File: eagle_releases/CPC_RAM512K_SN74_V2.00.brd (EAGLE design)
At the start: 99.1 x 81.3 mm, 19 parts

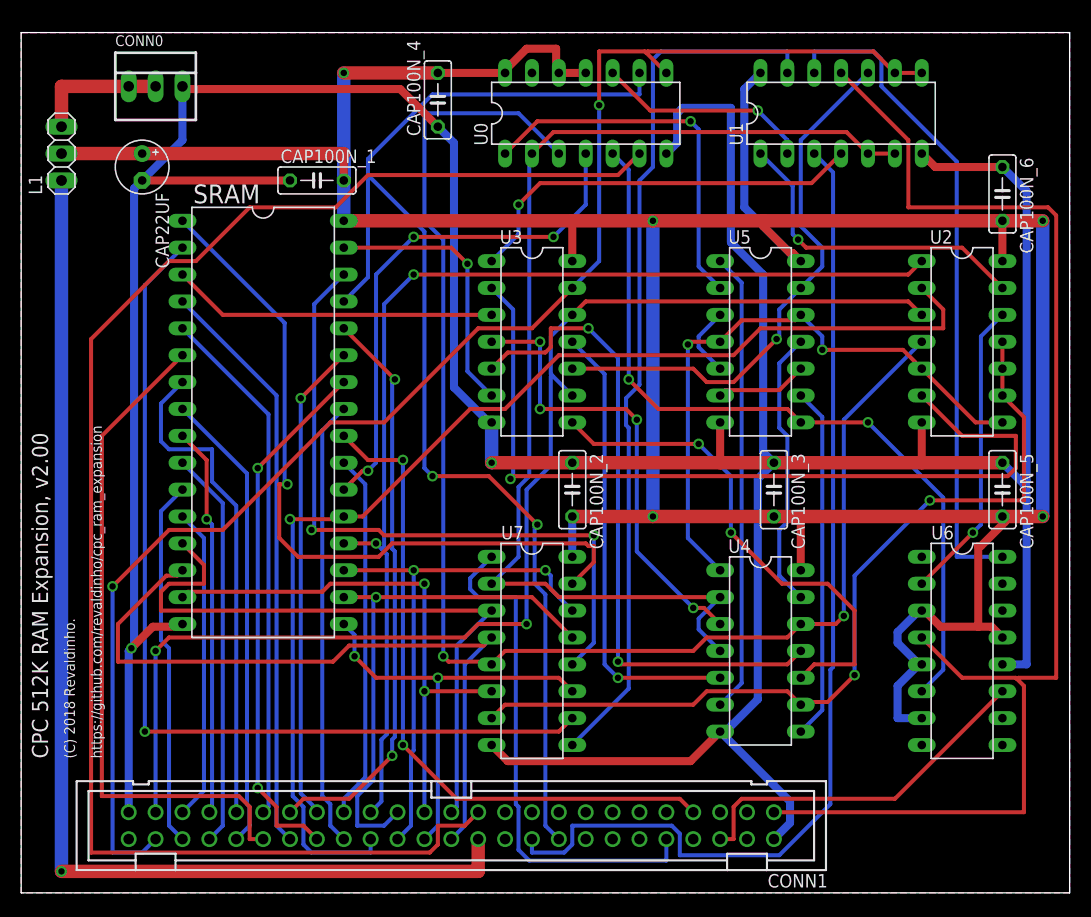
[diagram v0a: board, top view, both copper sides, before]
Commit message: Manual tweaks to 74XX board, mainly power improvements
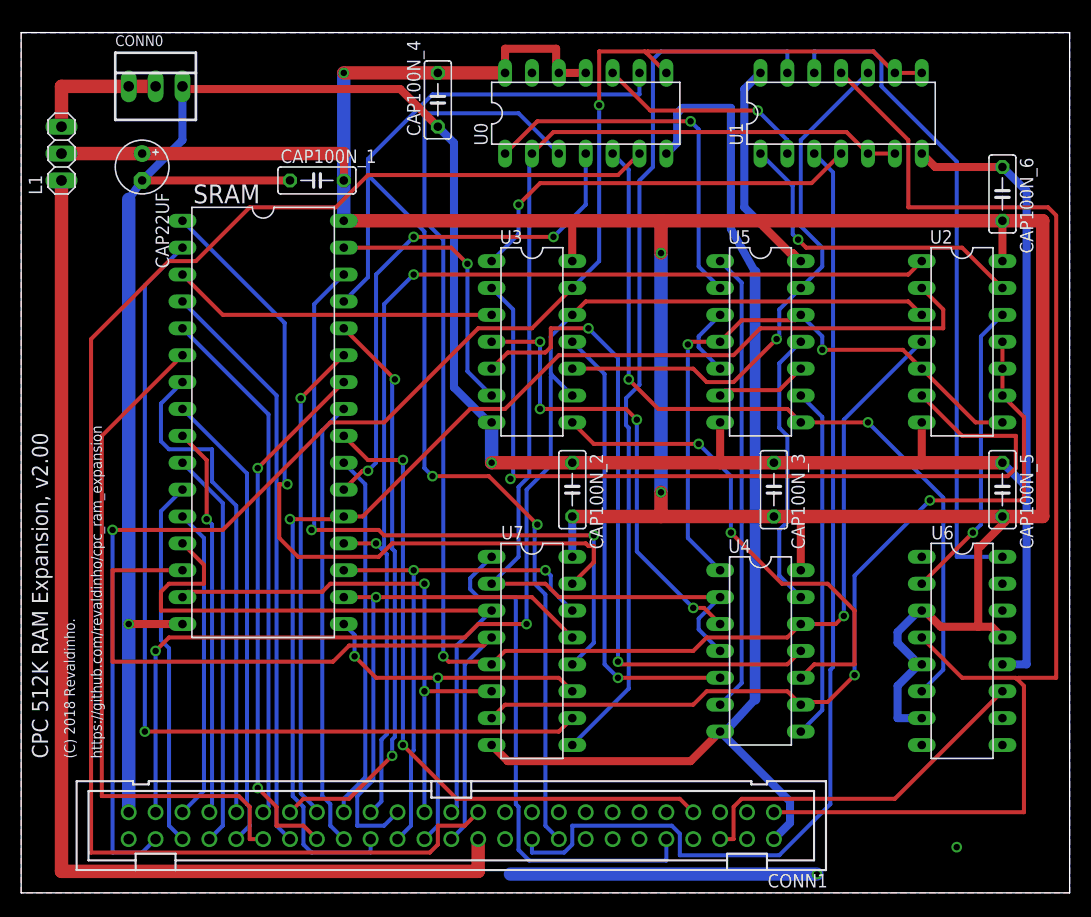
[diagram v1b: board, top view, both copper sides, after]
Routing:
- net VSS: track 376.9 -> 404.9 mm, vias 2 -> 4
- net D1: track 68.6 -> 72.6 mm
- net A15: track 142.4 -> 145.5 mm
- net VDD: track 316.9 -> 318.1 mm, vias 5 -> 3
- net VDD_CPC: vias 1 -> 0

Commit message: Add SN74 version release files
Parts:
- added CAP100N_7: (no value), resistor:C050-025X075
- moved CAP100N_4 64.8 mm to (92.7, 38.1), turned to 270 degrees
- moved CAP100N_5 61.3 mm to (38.1, 66.0)
- moved CAP100N_6 26.7 mm to (66.0, 66.0)
- moved U1 3.81 mm to (81.3, 73.7)
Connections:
- net VDD: now also CAP100N_7.2
- net VSS: now also CAP100N_7.1
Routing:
- net VDD_CPC: track 107.7 -> 216.4 mm
- net MREQ_B: track 146.8 -> 80.5 mm, vias 0 -> 1
- net VSS: track 404.9 -> 455.7 mm, vias 4 -> 11
- net A15: track 145.5 -> 193.3 mm, vias 2 -> 1
- net CLK: track 124.1 -> 87.9 mm, vias 0 -> 1
- net N16: track 80.7 -> 50.1 mm
- net N28: track 8.67 -> 37.2 mm
- net A5: track 55.0 -> 76.9 mm, vias 0 -> 1
- net D1: track 72.6 -> 52.9 mm, vias 0 -> 3
- net A10: track 36.8 -> 54.6 mm, vias 1 -> 0
- net N23: track 43.2 -> 60.1 mm
- net D6: track 105.3 -> 121.6 mm, vias 2 -> 1
- net RAMBLOCK_Q1: track 135.5 -> 120.9 mm
- net WR_B: track 118.2 -> 104.4 mm, vias 2 -> 3
- net N27: track 58.4 -> 72.0 mm, vias 2 -> 1
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
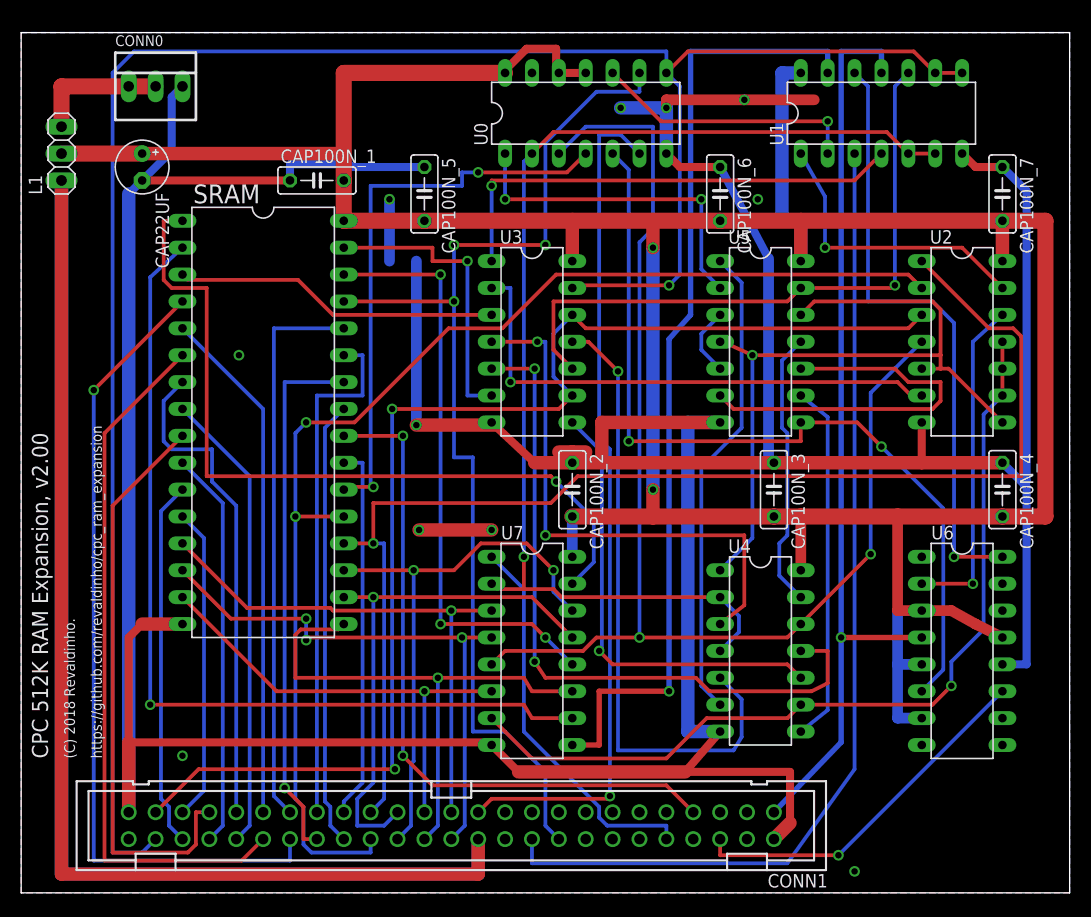
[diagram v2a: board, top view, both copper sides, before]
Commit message: Minor reworking of lower left corner to improve SRAM ground connection
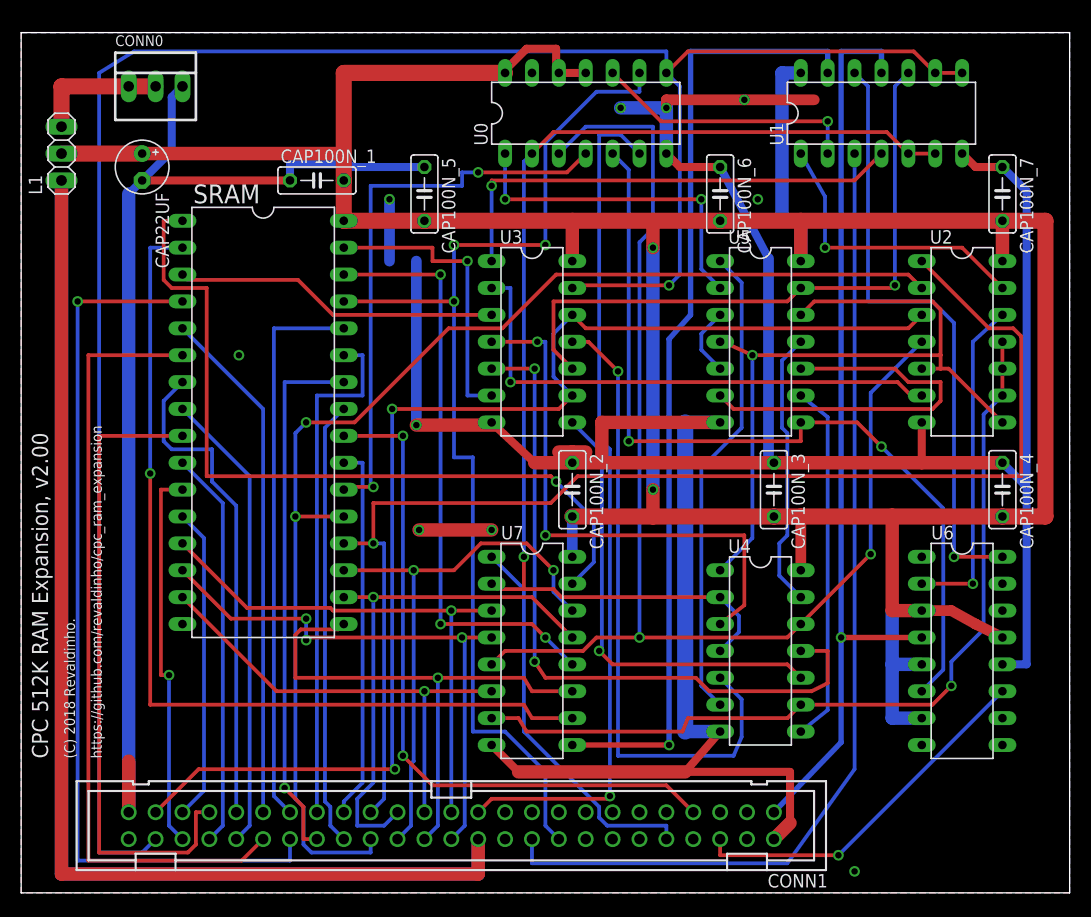
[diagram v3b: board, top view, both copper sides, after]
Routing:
- net VSS: track 455.7 -> 404.9 mm, vias 11 -> 10
- net A5: track 76.9 -> 84.8 mm
- net A7: track 66.6 -> 74.0 mm
- net A10: track 54.6 -> 61.0 mm
- net A15: track 193.3 -> 195.6 mm
- net VDD: track 314.2 -> 316.2 mm
- net RAMADRHI2: track 85.1 -> 86.8 mm
- net A13: track 34.7 -> 36.3 mm, vias 0 -> 1
- net RAMBLOCK_Q2: track 82.4 -> 80.8 mm
- net N23: track 60.1 -> 61.1 mm
